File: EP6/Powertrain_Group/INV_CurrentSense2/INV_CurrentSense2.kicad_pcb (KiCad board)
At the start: 2 copper layers, 41.8 x 43 mm, 43 parts, among them J2 5V&CAN, SW1 RESET, U1 ACS756xCB-100B-PFF, U2 STM32F103C8Tx, U3 XC6206PxxxMR, U4 TCAN1042VDRQ1

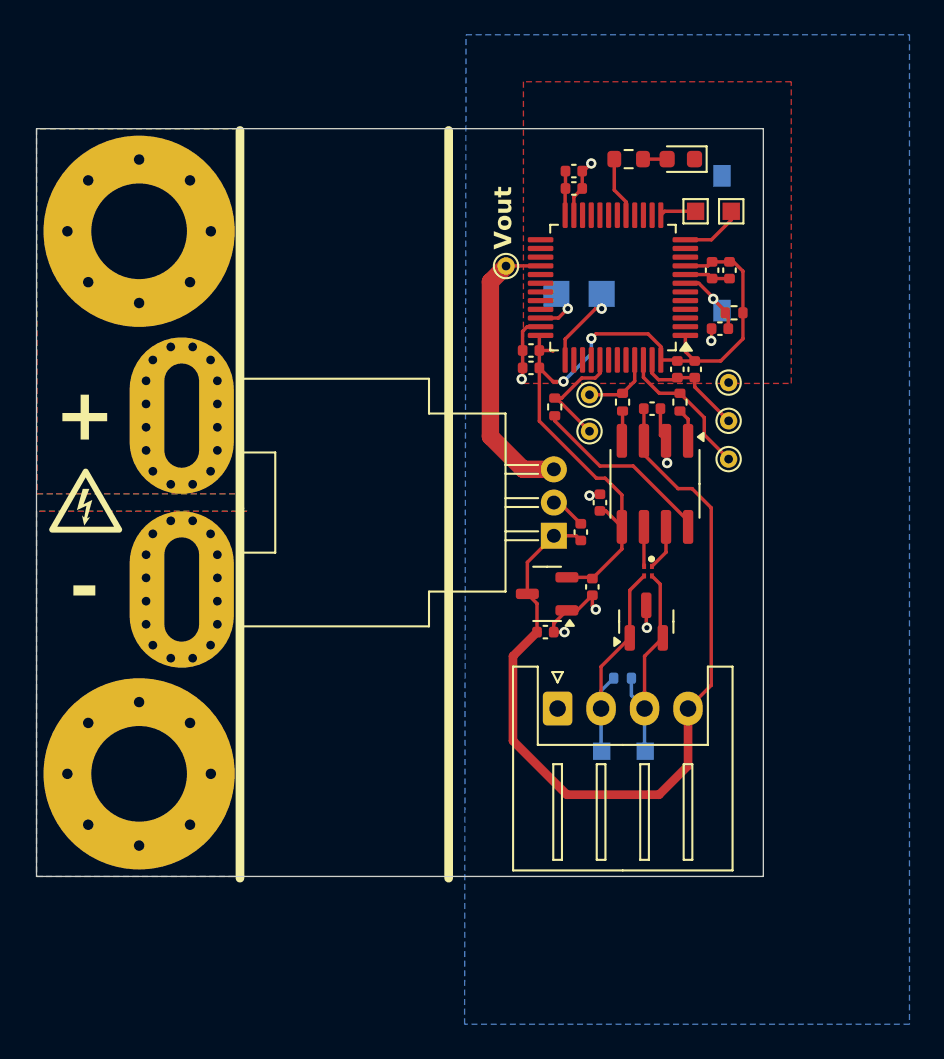
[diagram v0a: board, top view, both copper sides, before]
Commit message: batch update for JLCPCB 241117 again
will manufacture with JLC:
6S_BMS V1.0
INV_MainBoard_STM32
panelJLCPCB1117
 APPS_ROT_POT_onboard_XTR11x
 TCAN1042module
 INV_CurrentSense2
 INV_CurrentSense3

not yet sure to use JLC or Galexy: INV_DClinkCap1
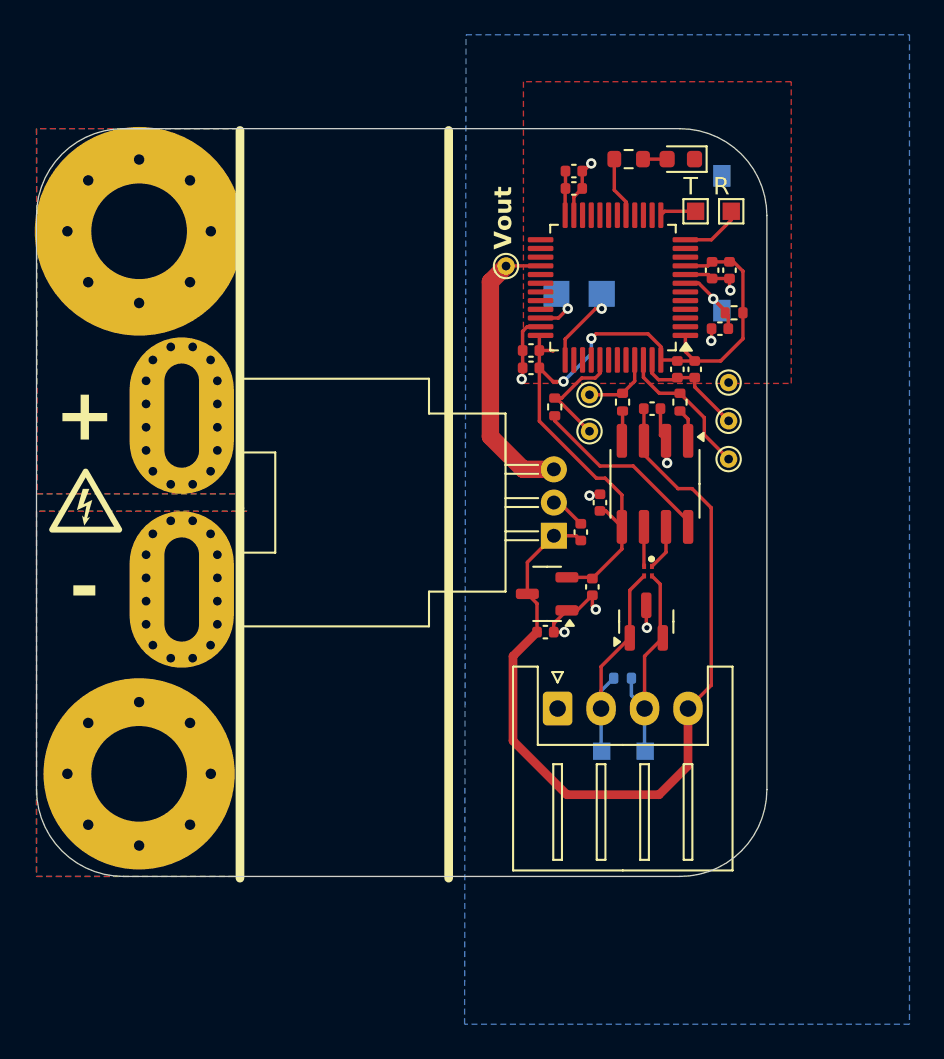
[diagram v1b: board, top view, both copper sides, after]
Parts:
- H1: footprint MountingHole:MountingHole_5.5mm_Pad_Via -> nturt_kicad_lib_EP6:MountingHole_5.5mm_Pad_Via_15mm_square; moved to B.Cu
- H2: value IP+ -> IP-
- turned H1 to 180 degrees
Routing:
- net GND: track 29.6 -> 30.3 mm, vias 8 -> 9
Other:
- board size 41.8 x 43 mm -> 42 x 43 mm
- board text added: "T R"
